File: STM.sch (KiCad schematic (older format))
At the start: 17 parts, among them J3 Micro_SD_Card_Det, J4 TagConnect_TC2030_SWD, Q9 AO3401A, SW8 POWER, U8 STM32L151C8Tx

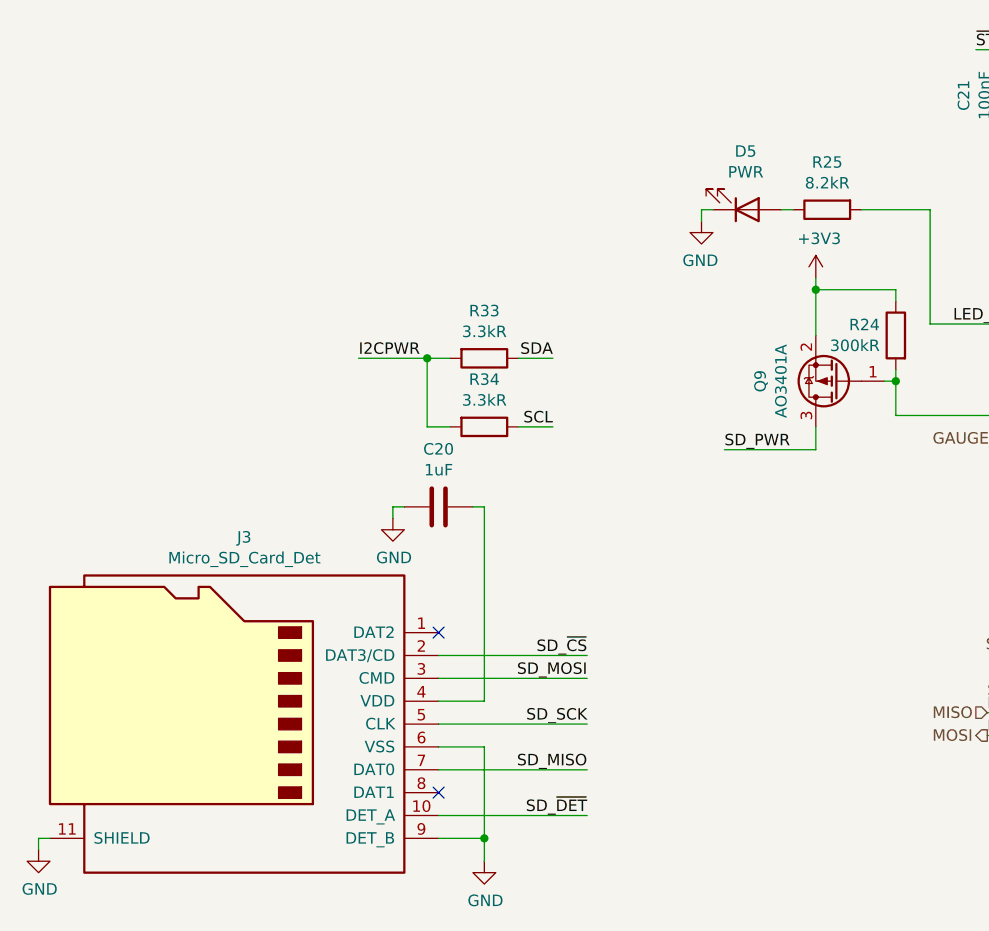
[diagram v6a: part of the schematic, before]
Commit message: route RGB LED
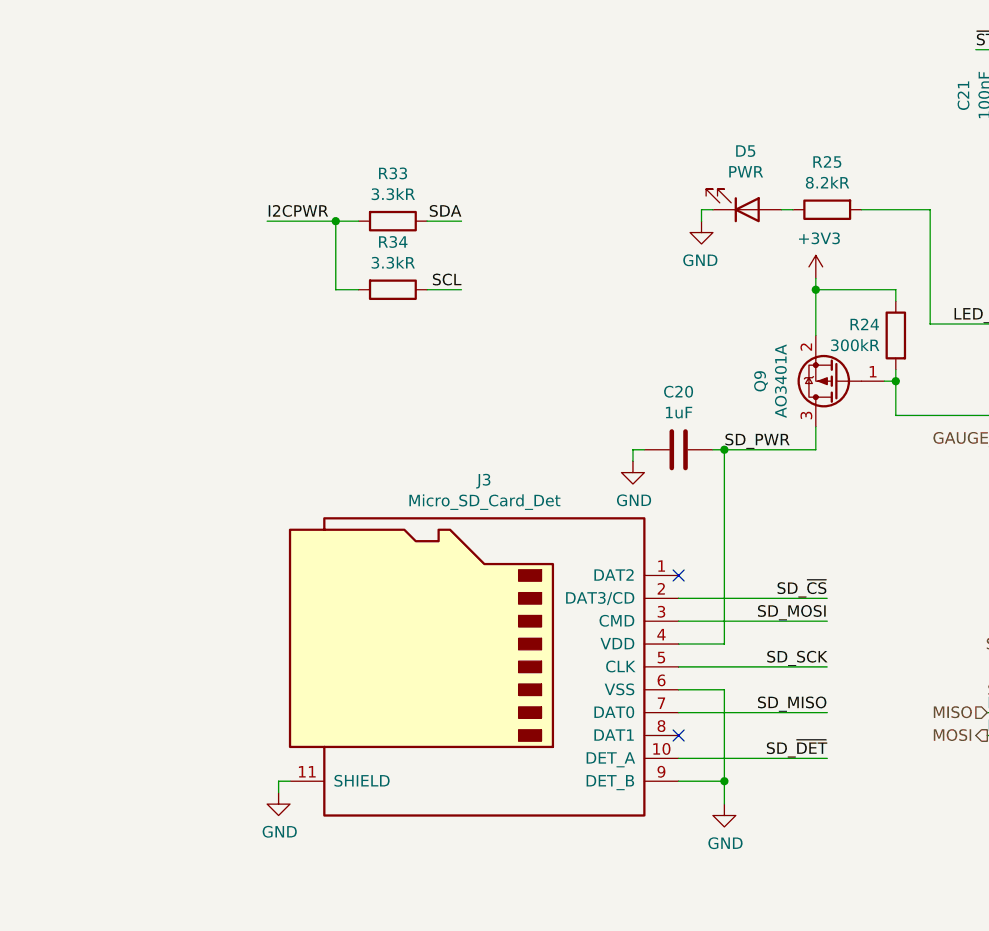
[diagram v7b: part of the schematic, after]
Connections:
- net SD_PWR: now also C20.1, J3.4 (VDD)
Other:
- moved on the sheet: C20, J3, R33, R34
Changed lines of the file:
@@
 L Connector:Micro_SD_Card_Det J?
 U 1 1 60D10208
-P 1650 5250
+P 2700 5000
 AR Path="/6051E9DC/60D10208" Ref="J?"  Part="1"
 AR Path="/60CF39C0/60D10208" Ref="J3"  Part="1"
-F 0 "J3" H 1600 6067 50  0000 C CNN
-F 1 "Micro_SD_Card_Det" H 1600 5976 50  0000 C CNN
-F 2 "Connector_Card_MicroSD:HOAUC_HYC77-TF09-200" H 3700 5950 50  0001 C CNN
-F 3 "https://www.hirose.com/product/en/download_file/key_name/DM3/category/Catalog/doc_file_id/49662/?file_category_id=4&item_id=195&is_series=1" H 1650 5350 50  0001 C CNN
-	1    1650 5250
+F 0 "J3" H 2650 5817 50  0000 C CNN
+F 1 "Micro_SD_Card_Det" H 2650 5726 50  0000 C CNN
+F 2 "Connector_Card_MicroSD:HOAUC_HYC77-TF09-200" H 4750 5700 50  0001 C CNN
+F 3 "https://www.hirose.com/product/en/download_file/key_name/DM3/category/Catalog/doc_file_id/49662/?file_category_id=4&item_id=195&is_series=1" H 2700 5100 50  0001 C CNN
+	1    2700 5000
 	-1   0    0    -1
 $EndComp
@@
 L power:GND #PWR?
 U 1 1 60D10218
-P 2750 5850
+P 3800 5600
 AR Path="/6051E9DC/60D10218" Ref="#PWR?"  Part="1"
 AR Path="/60CF39C0/60D10218" Ref="#PWR0115"  Part="1"
-F 0 "#PWR0115" H 2750 5600 50  0001 C CNN
-F 1 "GND" H 2755 5677 50  0000 C CNN
-F 2 "" H 2750 5850 50  0001 C CNN
-F 3 "" H 2750 5850 50  0001 C CNN
-	1    2750 5850
+F 0 "#PWR0115" H 3800 5350 50  0001 C CNN
+F 1 "GND" H 3805 5427 50  0000 C CNN
+F 2 "" H 3800 5600 50  0001 C CNN
+F 3 "" H 3800 5600 50  0001 C CNN
+	1    3800 5600
 	1    0    0    -1
 $EndComp
 Wire Wire Line
-	2750 5850 2750 5750
-Wire Wire Line
-	2750 5750 2550 5750
-Wire Wire Line
-	2750 5750 2750 5350
-Wire Wire Line
-	2750 5350 2550 5350
-Connection ~ 2750 5750
+	3800 5600 3800 5500
+Wire Wire Line
+	3800 5500 3600 5500
+Wire Wire Line
+	3800 5500 3800 5100
+Wire Wire Line
+	3800 5100 3600 5100
+Connection ~ 3800 5500
 $Comp
 L Device:C C?
 U 1 1 60D10227
-P 2550 4300
+P 3600 4050
 AR Path="/60D10227" Ref="C?"  Part="1"
 AR Path="/634EFCCB/60D10227" Ref="C?"  Part="1"
@@
 AR Path="/6051E9DC/60D10227" Ref="C?"  Part="1"
 AR Path="/60CF39C0/60D10227" Ref="C20"  Part="1"
-F 0 "C20" V 2298 4300 50  0000 C CNN
-F 1 "1uF" V 2389 4300 50  0000 C CNN
-F 2 "Capacitor_SMD:C_0402_1005Metric" H 2588 4150 50  0001 C CNN
-F 3 "~" H 2550 4300 50  0001 C CNN
-F 4 "C52923" V 2550 4300 50  0001 C CNN "LCSC"
-	1    2550 4300
+F 0 "C20" V 3348 4050 50  0000 C CNN
+F 1 "1uF" V 3439 4050 50  0000 C CNN
+F 2 "Capacitor_SMD:C_0402_1005Metric" H 3638 3900 50  0001 C CNN
+F 3 "~" H 3600 4050 50  0001 C CNN
+F 4 "C52923" V 3600 4050 50  0001 C CNN "LCSC"
+	1    3600 4050
 	0    1    1    0
 $EndComp
 Wire Wire Line
-	2550 5150 2750 5150
+	3600 4900 3800 4900
 $Comp
 L power:GND #PWR?
 U 1 1 60D1022E
-P 2350 4350
+P 3400 4100
 AR Path="/6051E9DC/60D1022E" Ref="#PWR?"  Part="1"
 AR Path="/60CF39C0/60D1022E" Ref="#PWR0116"  Part="1"
-F 0 "#PWR0116" H 2350 4100 50  0001 C CNN
-F 1 "GND" H 2355 4177 50  0000 C CNN
-F 2 "" H 2350 4350 50  0001 C CNN
-F 3 "" H 2350 4350 50  0001 C CNN
-	1    2350 4350
+F 0 "#PWR0116" H 3400 3850 50  0001 C CNN
+F 1 "GND" H 3405 3927 50  0000 C CNN
+F 2 "" H 3400 4100 50  0001 C CNN
+F 3 "" H 3400 4100 50  0001 C CNN
+	1    3400 4100
 	1    0    0    -1
 $EndComp
 Wire Wire Line
-	2350 4350 2350 4300
-Wire Wire Line
-	2350 4300 2400 4300
-Wire Wire Line
-	2750 4300 2700 4300
-Wire Wire Line
-	2750 4300 2750 5150
+	3400 4100 3400 4050
+Wire Wire Line
+	3400 4050 3450 4050
+Wire Wire Line
+	3800 4050 3750 4050
+Wire Wire Line
+	3800 4050 3800 4900
 $Comp
 L power:GND #PWR?
 U 1 1 60D10238
-P 800 5800
+P 1850 5550
 AR Path="/6051E9DC/60D10238" Ref="#PWR?"  Part="1"
 AR Path="/60CF39C0/60D10238" Ref="#PWR0117"  Part="1"
-F 0 "#PWR0117" H 800 5550 50  0001 C CNN
-F 1 "GND" H 805 5627 50  0000 C CNN
-F 2 "" H 800 5800 50  0001 C CNN
-F 3 "" H 800 5800 50  0001 C CNN
-	1    800  5800
+F 0 "#PWR0117" H 1850 5300 50  0001 C CNN
+F 1 "GND" H 1855 5377 50  0000 C CNN
+F 2 "" H 1850 5550 50  0001 C CNN
+F 3 "" H 1850 5550 50  0001 C CNN
+	1    1850 5550
 	1    0    0    -1
 $EndComp
 Wire Wire Line
-	800  5800 800  5750
-Wire Wire Line
-	800  5750 850  5750
+	1850 5550 1850 5500
+Wire Wire Line
+	1850 5500 1900 5500
 $Comp
 L Transistor_FET:AO3401A Q?
@@
 	4550 3900 4550 3750
 Connection ~ 4550 3750
-NoConn ~ 2550 4850
-NoConn ~ 2550 5550
+NoConn ~ 3600 4600
+NoConn ~ 3600 5300
 Text HLabel 7150 4000 2    50   Output ~ 0
 PWR_EN
@@
 L Device:R R?
 U 1 1 611AA57E
-P 2750 3650
+P 2350 3050
 AR Path="/611AA57E" Ref="R?"  Part="1"
 AR Path="/60CF39C0/611AA57E" Ref="R33"  Part="1"
-F 0 "R33" V 2543 3650 50  0000 C CNN
-F 1 "3.3kR" V 2634 3650 50  0000 C CNN
-F 2 "Resistor_SMD:R_0402_1005Metric" V 2680 3650 50  0001 C CNN
-F 3 "~" H 2750 3650 50  0001 C CNN
-F 4 "C25890" V 2750 3650 50  0001 C CNN "LCSC"
-	1    2750 3650
+F 0 "R33" V 2143 3050 50  0000 C CNN
+F 1 "3.3kR" V 2234 3050 50  0000 C CNN
+F 2 "Resistor_SMD:R_0402_1005Metric" V 2280 3050 50  0001 C CNN
+F 3 "~" H 2350 3050 50  0001 C CNN
+F 4 "C25890" V 2350 3050 50  0001 C CNN "LCSC"
+	1    2350 3050
 	0    1    1    0
 $EndComp
@@
 L Device:R R?
 U 1 1 611AE5AD
-P 2750 3950
+P 2350 3350
 AR Path="/611AE5AD" Ref="R?"  Part="1"
 AR Path="/60CF39C0/611AE5AD" Ref="R34"  Part="1"
-F 0 "R34" V 2543 3950 50  0000 C CNN
-F 1 "3.3kR" V 2634 3950 50  0000 C CNN
-F 2 "Resistor_SMD:R_0402_1005Metric" V 2680 3950 50  0001 C CNN
-F 3 "~" H 2750 3950 50  0001 C CNN
-F 4 "C25890" V 2750 3950 50  0001 C CNN "LCSC"
-	1    2750 3950
+F 0 "R34" V 2143 3350 50  0000 C CNN
+F 1 "3.3kR" V 2234 3350 50  0000 C CNN
+F 2 "Resistor_SMD:R_0402_1005Metric" V 2280 3350 50  0001 C CNN
+F 3 "~" H 2350 3350 50  0001 C CNN
+F 4 "C25890" V 2350 3350 50  0001 C CNN "LCSC"
+	1    2350 3350
 	0    1    1    0
 $EndComp
 Wire Wire Line
-	2600 3950 2500 3950
-Wire Wire Line
-	2500 3950 2500 3650
-Wire Wire Line
-	2500 3650 2600 3650
-Connection ~ 2500 3650
-Text Label 2200 3650 0    50   ~ 0
+	2200 3350 2100 3350
+Wire Wire Line
+	2100 3350 2100 3050
+Wire Wire Line
+	2100 3050 2200 3050
+Connection ~ 2100 3050
+Text Label 1800 3050 0    50   ~ 0
 I2CPWR
 Wire Wire Line
-	2200 3650 2500 3650
-Wire Wire Line
-	2900 3650 3050 3650
-Text Label 3050 3650 2    50   ~ 0
+	1800 3050 2100 3050
+Wire Wire Line
+	2500 3050 2650 3050
+Text Label 2650 3050 2    50   ~ 0
 SDA
 Wire Wire Line
-	2900 3950 3050 3950
-Text Label 3050 3950 2    50   ~ 0
+	2500 3350 2650 3350
+Text Label 2650 3350 2    50   ~ 0
 SCL
 Wire Wire Line
@@
 SD_PWR
 Wire Wire Line
-	2550 5650 3200 5650
-Text Label 3200 5650 2    50   ~ 0
+	3600 5400 4250 5400
+Text Label 4250 5400 2    50   ~ 0
 SD_~DET
-Text Label 3200 5450 2    50   ~ 0
+Text Label 4250 5200 2    50   ~ 0
 SD_MISO
 Wire Wire Line
-	2550 4950 3200 4950
-Text Label 3200 4950 2    50   ~ 0
+	3600 4700 4250 4700
+Text Label 4250 4700 2    50   ~ 0
 SD_~CS
-Text Label 3200 5050 2    50   ~ 0
+Text Label 4250 4800 2    50   ~ 0
 SD_MOSI
 Wire Wire Line
-	2550 5050 3200 5050
-Wire Wire Line
-	2550 5450 3200 5450
-Text Label 3200 5250 2    50   ~ 0
+	3600 4800 4250 4800
+Wire Wire Line
+	3600 5200 4250 5200
+Text Label 4250 5000 2    50   ~ 0
 SD_SCK
 Wire Wire Line
-	3200 5250 2550 5250
+	4250 5000 3600 5000
 Wire Wire Line
 	7000 4500 6650 4500
@@
 Text Notes 5950 4200 2    50   ~ 0
 ~JTRST
+Connection ~ 3800 4050
 $EndSCHEMATC

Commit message: Add support for GBA D-Pad mounting
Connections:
- net DOWN: now also U8.43 (PB7); no longer U8.41 (PB5)
- net UP: now also U8.41 (PB5); no longer U8.43 (PB7)
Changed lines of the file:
@@
 $Descr A4 11693 8268
 encoding utf-8
-Sheet 4 4
+Sheet 4 23
 Title ""
 Date ""
@@
 B
 Wire Wire Line
-	5450 4500 5150 4500
-Text HLabel 5150 4500 0    50   Input ~ 0
+	5450 4300 5150 4300
+Text HLabel 5150 4300 0    50   Input ~ 0
 UP
 Text HLabel 5300 4400 0    50   Input ~ 0
@@
 Wire Wire Line
 	5300 4400 5450 4400
-Text HLabel 5300 4300 0    50   Input ~ 0
-DOWN
-Wire Wire Line
-	5300 4300 5450 4300
 Text HLabel 5300 4100 0    50   Input ~ 0
 RIGHT
@@
 ~JTRST
 Connection ~ 3800 4050
+Wire Wire Line
+	5300 4500 5450 4500
+Text HLabel 5300 4500 0    50   Input ~ 0
+DOWN
 $EndSCHEMATC
